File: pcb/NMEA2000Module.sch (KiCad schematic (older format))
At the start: 45 parts, among them IC1 MCP2562FD, K1 1W1, P1 PULSE_IN, P3 TERM_R, P4 CAN, P7 I2C1, P9 ANALOG IN, SW1 BT Enable, U1 74HC14, U2 ESP32Dev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

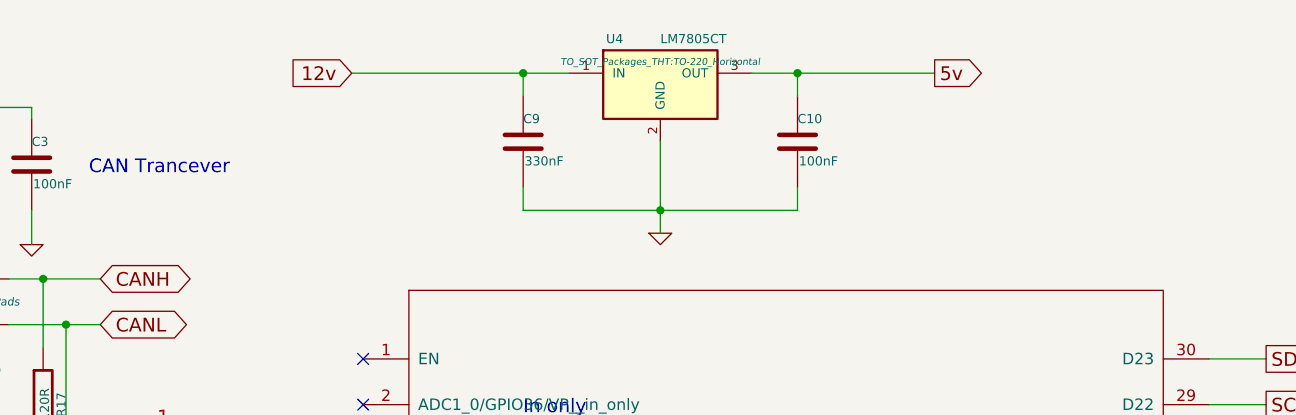
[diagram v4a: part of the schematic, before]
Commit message: Dropped oil pressure, teste fuel level
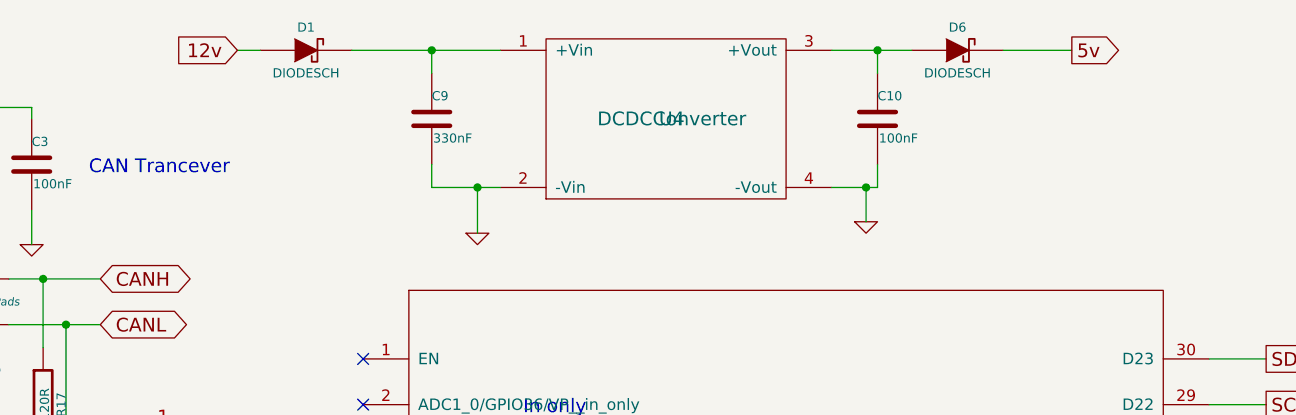
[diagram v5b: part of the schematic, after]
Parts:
- removed U4: LM7805CT, TO_SOT_Packages_THT:TO-220_Horizontal, symbol LM7805CT
- added D1, D6: DIODESCH, Resistors_ThroughHole:Resistor_Horizontal_RM7mm, symbol DIODESCH
- added U4: DCDCConverter, Divers:DC-DC-Converter, symbol DCDCConverter
- D2, D3, D4, D5: footprint Resistors_ThroughHole:Resistor_Horizontal_RM7mm -> TO_SOT_Packages_SMD:SOT-23
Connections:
- net 12v: now also D1.1 (A); no longer C9.1
- net 5v: now also D6.2 (K); no longer C10.1
- net GND: now also U4.2 (-Vin), U4.4 (-Vout)
- new net: C9.1, D1.2 (K), U4.1 (+Vin)
- new net: C10.1, D6.1 (A), U4.3 (+Vout)
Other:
- moved on the sheet: C10, C9
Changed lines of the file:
@@
 Text GLabel 3450 5050 0    60   Input ~ 0
 5v
-Text GLabel 6200 900  2    60   Output ~ 0
+Text GLabel 6800 800  2    60   Output ~ 0
 5v
 $Comp
@@
 Text GLabel 10500 4100 2    60   BiDi ~ 0
 CANL
-Text GLabel 3650 900  0    60   Input ~ 0
+Text GLabel 3150 800  0    60   Input ~ 0
 12v
 $Comp
 L GND #PWR014
 U 1 1 6019290E
-P 5000 1600
-F 0 "#PWR014" H 5000 1600 30  0001 C CNN
-F 1 "GND" H 5000 1530 30  0001 C CNN
-F 2 "" H 5000 1600 60  0001 C CNN
-F 3 "" H 5000 1600 60  0001 C CNN
-	1    5000 1600
+P 4200 1600
+F 0 "#PWR014" H 4200 1600 30  0001 C CNN
+F 1 "GND" H 4200 1530 30  0001 C CNN
+F 2 "" H 4200 1600 60  0001 C CNN
+F 3 "" H 4200 1600 60  0001 C CNN
+	1    4200 1600
 	1    0    0    -1
 $EndComp
@@
 F 0 "D3" H 1000 7500 40  0000 C CNN
 F 1 "DIODE" H 1000 7300 40  0000 C CNN
-F 2 "Resistors_ThroughHole:Resistor_Horizontal_RM7mm" H 1000 7400 60  0001 C CNN
+F 2 "TO_SOT_Packages_SMD:SOT-23" H 1000 7400 60  0001 C CNN
 F 3 "" H 1000 7400 60  0000 C CNN
 	1    1000 7400
@@
 F 0 "D2" H 1000 6850 40  0000 C CNN
 F 1 "DIODE" H 1000 6650 40  0000 C CNN
-F 2 "Resistors_ThroughHole:Resistor_Horizontal_RM7mm" H 1000 6750 60  0001 C CNN
+F 2 "TO_SOT_Packages_SMD:SOT-23" H 1000 6750 60  0001 C CNN
 F 3 "" H 1000 6750 60  0000 C CNN
 	1    1000 6750
@@
 F 0 "D5" H 3450 7500 40  0000 C CNN
 F 1 "DIODE" H 3450 7300 40  0000 C CNN
-F 2 "Resistors_ThroughHole:Resistor_Horizontal_RM7mm" H 3450 7400 60  0001 C CNN
+F 2 "TO_SOT_Packages_SMD:SOT-23" H 3450 7400 60  0001 C CNN
 F 3 "" H 3450 7400 60  0000 C CNN
 	1    3450 7400
@@
 F 0 "D4" H 3450 6900 40  0000 C CNN
 F 1 "DIODE" H 3450 6700 40  0000 C CNN
-F 2 "Resistors_ThroughHole:Resistor_Horizontal_RM7mm" H 3450 6800 60  0001 C CNN
+F 2 "TO_SOT_Packages_SMD:SOT-23" H 3450 6800 60  0001 C CNN
 F 3 "" H 3450 6800 60  0000 C CNN
 	1    3450 6800
@@
 	2650 3600 2500 3600
 Wire Wire Line
-	3650 900  4600 900
-Wire Wire Line
-	5400 900  6200 900
-Wire Wire Line
 	9950 4750 9950 4800
 Wire Wire Line
@@
 L C C9
 U 1 1 603DE009
-P 4400 1200
-F 0 "C9" H 4400 1300 40  0000 L CNN
-F 1 "330nF" H 4406 1115 40  0000 L CNN
-F 2 "Capacitors_SMD:C_0805_HandSoldering" H 4438 1050 30  0001 C CNN
-F 3 "" H 4400 1200 60  0000 C CNN
-	1    4400 1200
+P 4000 1100
+F 0 "C9" H 4000 1200 40  0000 L CNN
+F 1 "330nF" H 4006 1015 40  0000 L CNN
+F 2 "Capacitors_SMD:C_0805_HandSoldering" H 4038 950 30  0001 C CNN
+F 3 "" H 4000 1100 60  0000 C CNN
+	1    4000 1100
 	1    0    0    -1
 $EndComp
@@
 L C C10
 U 1 1 603DE0BF
-P 5600 1200
-F 0 "C10" H 5600 1300 40  0000 L CNN
-F 1 "100nF" H 5606 1115 40  0000 L CNN
-F 2 "Capacitors_SMD:C_0805_HandSoldering" H 5638 1050 30  0001 C CNN
-F 3 "" H 5600 1200 60  0000 C CNN
-	1    5600 1200
-	1    0    0    -1
-$EndComp
-Wire Wire Line
-	4400 1400 4400 1500
-Wire Wire Line
-	4400 1500 5600 1500
-Wire Wire Line
-	5600 1500 5600 1400
-Wire Wire Line
-	5000 1200 5000 1600
-Connection ~ 5000 1500
-Wire Wire Line
-	4400 1000 4400 900
-Connection ~ 4400 900
-Wire Wire Line
-	5600 1000 5600 900
-Connection ~ 5600 900
-$Comp
-L LM7805CT U4
-U 1 1 603DFA56
-P 5000 950
-F 0 "U4" H 4800 1150 40  0000 C CNN
-F 1 "LM7805CT" H 5000 1150 40  0000 L CNN
-F 2 "TO_SOT_Packages_THT:TO-220_Horizontal" H 5000 1050 30  0000 C CIN
-F 3 "" H 5000 950 60  0000 C CNN
-	1    5000 950
+P 5950 1100
+F 0 "C10" H 5950 1200 40  0000 L CNN
+F 1 "100nF" H 5956 1015 40  0000 L CNN
+F 2 "Capacitors_SMD:C_0805_HandSoldering" H 5988 950 30  0001 C CNN
+F 3 "" H 5950 1100 60  0000 C CNN
+	1    5950 1100
 	1    0    0    -1
 $EndComp
@@
 Wire Wire Line
 	3550 3550 3700 3550
+$Comp
+L DCDCConverter U4
+U 1 1 6049D818
+P 5050 1100
+F 0 "U4" H 5050 1100 60  0000 C CNN
+F 1 "DCDCConverter" H 5050 1100 60  0000 C CNN
+F 2 "Divers:DC-DC-Converter" H 5050 1100 60  0001 C CNN
+F 3 "" H 5050 1100 60  0001 C CNN
+	1    5050 1100
+	1    0    0    -1
+$EndComp
+Wire Wire Line
+	4300 800  3650 800
+Wire Wire Line
+	4000 900  4000 800
+Connection ~ 4000 800
+Wire Wire Line
+	5950 900  5950 800
+Wire Wire Line
+	5750 800  6100 800
+Wire Wire Line
+	5950 1300 5950 1400
+Wire Wire Line
+	5950 1400 5750 1400
+Wire Wire Line
+	4300 1400 4000 1400
+Wire Wire Line
+	4000 1400 4000 1300
+Wire Wire Line
+	4200 1600 4200 1400
+Connection ~ 4200 1400
+$Comp
+L DIODESCH D1
+U 1 1 6049E8CA
+P 3450 800
+F 0 "D1" H 3450 900 40  0000 C CNN
+F 1 "DIODESCH" H 3450 700 40  0000 C CNN
+F 2 "Resistors_ThroughHole:Resistor_Horizontal_RM7mm" H 3450 800 60  0001 C CNN
+F 3 "" H 3450 800 60  0000 C CNN
+	1    3450 800
+	1    0    0    -1
+$EndComp
+$Comp
+L DIODESCH D6
+U 1 1 6049E984
+P 6300 800
+F 0 "D6" H 6300 900 40  0000 C CNN
+F 1 "DIODESCH" H 6300 700 40  0000 C CNN
+F 2 "Resistors_ThroughHole:Resistor_Horizontal_RM7mm" H 6300 800 60  0001 C CNN
+F 3 "" H 6300 800 60  0000 C CNN
+	1    6300 800
+	1    0    0    -1
+$EndComp
+Connection ~ 5950 800
+Wire Wire Line
+	6500 800  6800 800
+Wire Wire Line
+	3250 800  3150 800
+$Comp
+L GND #PWR018
+U 1 1 6049ED9D
+P 5900 1550
+F 0 "#PWR018" H 5900 1550 30  0001 C CNN
+F 1 "GND" H 5900 1480 30  0001 C CNN
+F 2 "" H 5900 1550 60  0001 C CNN
+F 3 "" H 5900 1550 60  0001 C CNN
+	1    5900 1550
+	1    0    0    -1
+$EndComp
+Wire Wire Line
+	5900 1550 5900 1400
+Connection ~ 5900 1400
 $EndSCHEMATC

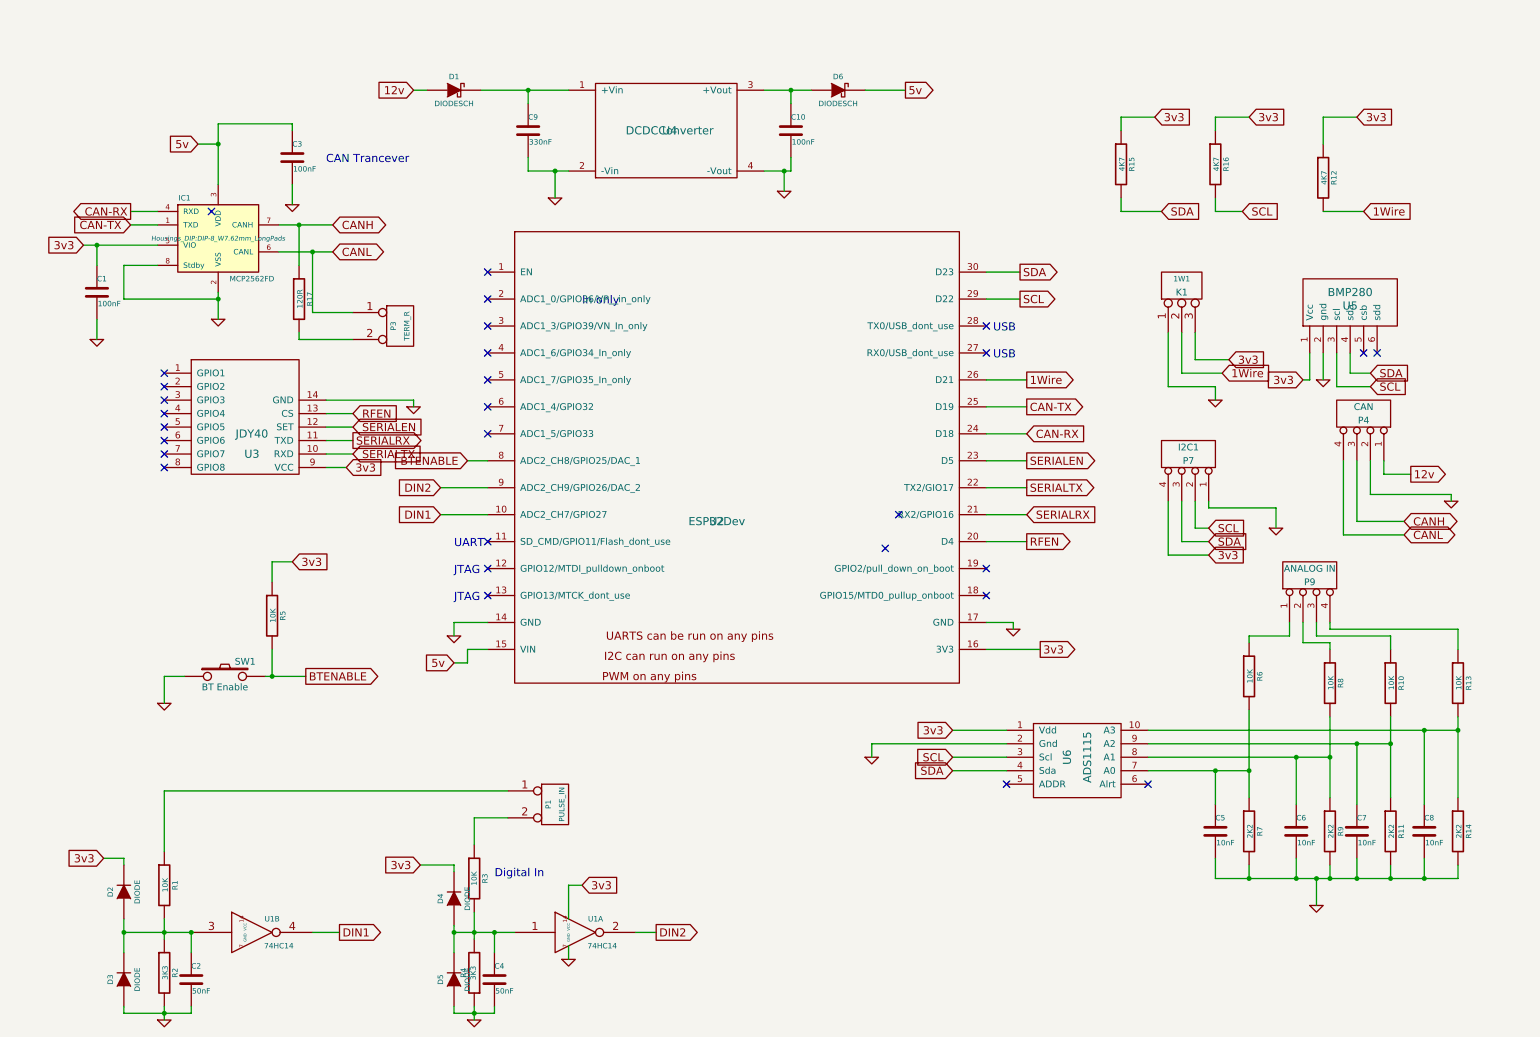
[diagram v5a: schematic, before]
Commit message: Added better support for simulation and alarms
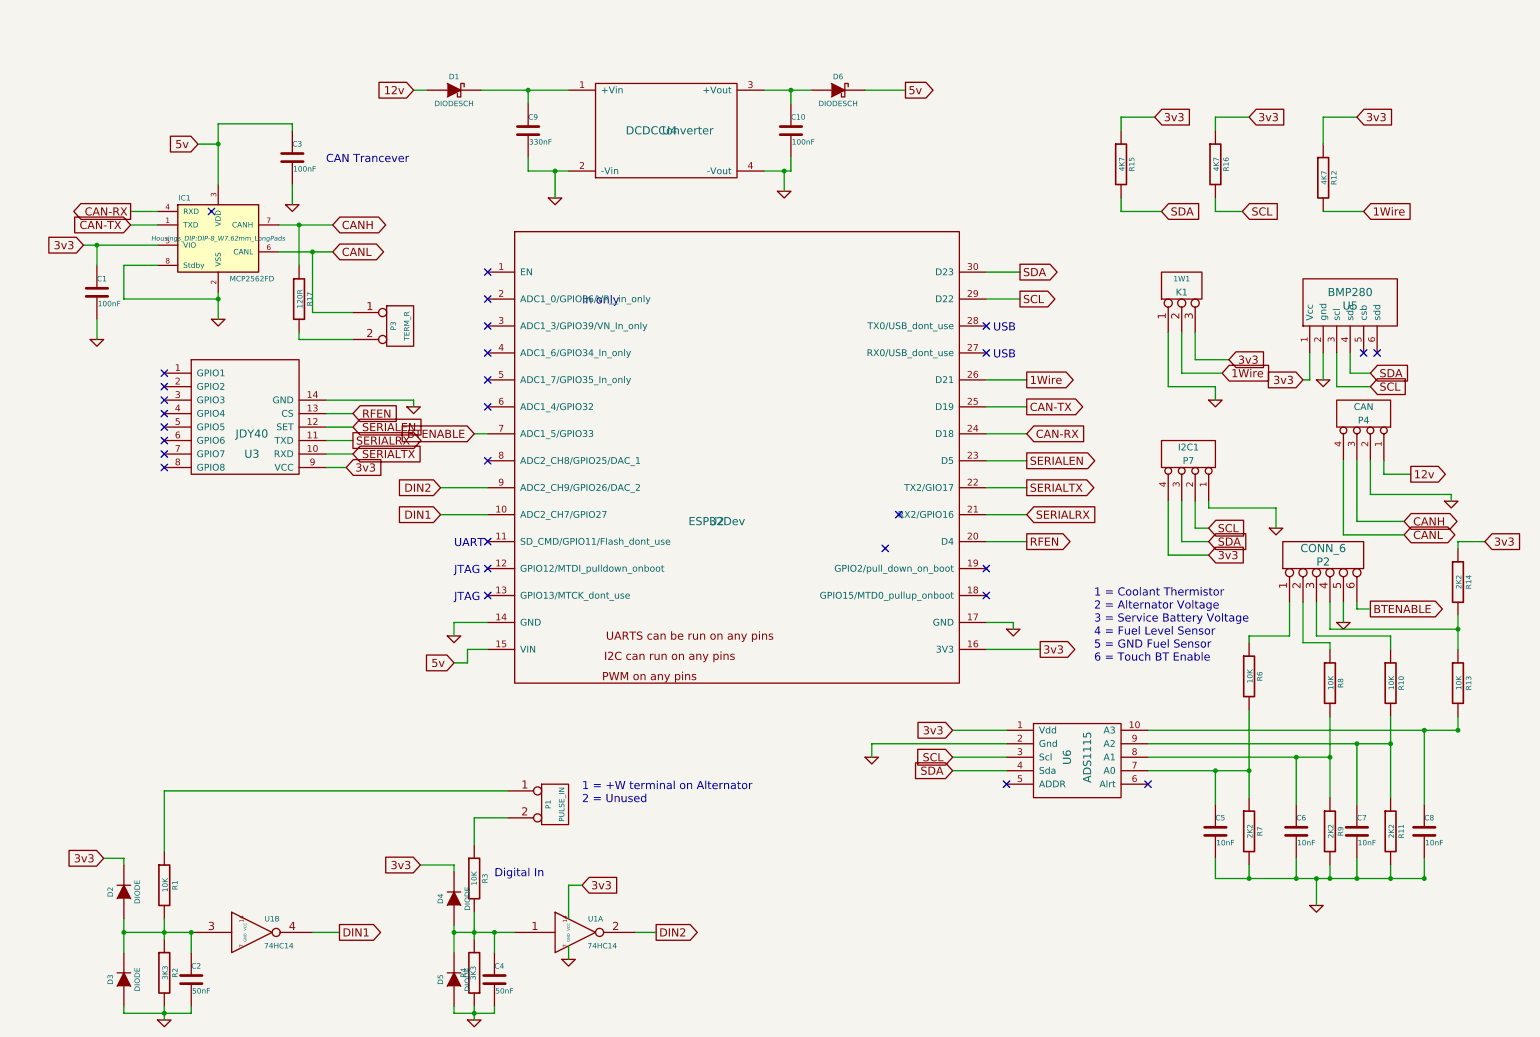
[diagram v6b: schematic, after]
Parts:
- removed P9: ANALOG IN, Pin_Headers:Pin_Header_Straight_1x04_Pitch2.54mm, symbol CONN_4
- removed R5: 10K, Resistors_SMD:R_0805_HandSoldering, symbol R
- removed SW1: BT Enable, Buttons_Switches_ThroughHole:SW_PUSH_6mm, symbol SW_PUSH
- added P2: CONN_6, Pin_Headers:Pin_Header_Straight_1x06_Pitch2.54mm, symbol CONN_6
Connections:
- net 3v3: now also R14.1
- net BTENABLE: now also U2.7 (ADC1_5/GPIO33), P2.6; no longer U2.8 (ADC2_CH8/GPIO25/DAC_1)
- net GND: now also P2.5; no longer R14.2
- net at R8.1: now also P2.2
- net at R10.1: now also P2.3
- net at R13.1: now also R14.2, P2.4
- net at C8.1, R13.2, U6.10 (A3): no longer R14.1
- net at R6.1: now also P2.1
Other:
- note added: "1 = +W terminal on Alternator\n2 = Unused"
- note added: "1 = Coolant Thermistor\n2 = Alternator Voltage\n3 = Service Battery Voltage\n4 = Fuel Level Sensor\n5 = GND Fuel Sensor\n6 = Touch BT Enable\n"
- moved on the sheet: R14
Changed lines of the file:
@@
-$EndComp
-$Comp
-L CONN_4 P9
-U 1 1 5F40035E
-P 9800 4400
-F 0 "P9" V 9750 4400 50  0000 C CNN
-F 1 "ANALOG IN" V 9850 4400 50  0000 C CNN
-F 2 "Pin_Headers:Pin_Header_Straight_1x04_Pitch2.54mm" H 9800 4400 60  0001 C CNN
-F 3 "" H 9800 4400 60  0001 C CNN
-	1    9800 4400
-	0    -1   -1   0
 $EndComp
 $Comp
@@
 NoConn ~ 7400 4550
 NoConn ~ 7400 4350
-NoConn ~ 3700 3350
 NoConn ~ 3700 3150
 NoConn ~ 3700 2950
@@
 L R R14
 U 1 1 60181295
-P 10900 6300
-F 0 "R14" V 10980 6300 40  0000 C CNN
-F 1 "2K2" V 10907 6301 40  0000 C CNN
-F 2 "Resistors_SMD:R_0805_HandSoldering" V 10830 6300 30  0001 C CNN
-F 3 "" H 10900 6300 30  0000 C CNN
-	1    10900 6300
+P 10900 4450
+F 0 "R14" V 10980 4450 40  0000 C CNN
+F 1 "2K2" V 10907 4451 40  0000 C CNN
+F 2 "Resistors_SMD:R_0805_HandSoldering" V 10830 4450 30  0001 C CNN
+F 3 "" H 10900 4450 30  0000 C CNN
+	1    10900 4450
 	1    0    0    -1
 $EndComp
@@
 	2650 3600 2500 3600
 Wire Wire Line
-	9950 4750 9950 4800
+	9950 4600 9950 4800
 Wire Wire Line
 	9950 4800 10900 4800
 Wire Wire Line
-	10900 4800 10900 4950
-Wire Wire Line
-	10400 4950 10400 4850
-Wire Wire Line
-	10400 4850 9850 4850
-Wire Wire Line
-	9850 4850 9850 4750
+	10900 4700 10900 4950
+Wire Wire Line
+	10400 4850 10400 4950
+Wire Wire Line
+	9850 4600 9850 4850
 Wire Wire Line
 	9950 4950 9950 4900
@@
 	9950 4900 9750 4900
 Wire Wire Line
-	9750 4900 9750 4750
+	9750 4900 9750 4600
 Wire Wire Line
 	9350 4900 9350 4850
@@
 	9350 4850 9650 4850
 Wire Wire Line
-	9650 4850 9650 4750
+	9650 4850 9650 4600
 Wire Wire Line
 	9100 6500 9100 6650
 Wire Wire Line
-	9100 6650 10900 6650
-Wire Wire Line
-	10900 6650 10900 6550
+	9100 6650 10650 6650
 Wire Wire Line
 	10650 6650 10650 6500
@@
 	8600 5550 10900 5550
 Wire Wire Line
-	10900 5450 10900 6050
+	10900 5550 10900 5450
 Wire Wire Line
 	8600 5650 10400 5650
@@
 	1    0    0    -1
 $EndComp
-$Comp
-L SW_PUSH SW1
-U 1 1 6049C3C9
-P 1750 5150
-F 0 "SW1" H 1900 5260 50  0000 C CNN
-F 1 "BT Enable" H 1750 5070 50  0000 C CNN
-F 2 "Buttons_Switches_ThroughHole:SW_PUSH_6mm" H 1750 5150 60  0001 C CNN
-F 3 "" H 1750 5150 60  0000 C CNN
-	1    1750 5150
-	1    0    0    -1
-$EndComp
-$Comp
-L R R5
-U 1 1 6049C957
-P 2100 4700
-F 0 "R5" V 2180 4700 40  0000 C CNN
-F 1 "10K" V 2107 4701 40  0000 C CNN
-F 2 "Resistors_SMD:R_0805_HandSoldering" V 2030 4700 30  0001 C CNN
-F 3 "" H 2100 4700 30  0000 C CNN
-	1    2100 4700
-	1    0    0    -1
-$EndComp
-$Comp
-L GND #PWR017
-U 1 1 6049C9FC
-P 1300 5350
-F 0 "#PWR017" H 1300 5350 30  0001 C CNN
-F 1 "GND" H 1300 5280 30  0001 C CNN
-F 2 "" H 1300 5350 60  0001 C CNN
-F 3 "" H 1300 5350 60  0001 C CNN
-	1    1300 5350
-	1    0    0    -1
-$EndComp
-Wire Wire Line
-	1450 5150 1300 5150
-Wire Wire Line
-	1300 5150 1300 5350
-Wire Wire Line
-	2050 5150 2350 5150
-Wire Wire Line
-	2100 5150 2100 4950
-Text GLabel 2250 4300 2    60   Input ~ 0
-3v3
-Wire Wire Line
-	2100 4450 2100 4300
-Wire Wire Line
-	2100 4300 2250 4300
-Text GLabel 3550 3550 0    60   Input ~ 0
+Text GLabel 3600 3350 0    60   Input ~ 0
 BTENABLE
-Text GLabel 2350 5150 2    60   Output ~ 0
+Text GLabel 10250 4650 2    60   Output ~ 0
 BTENABLE
-Connection ~ 2100 5150
-Wire Wire Line
-	3550 3550 3700 3550
 $Comp
 L DCDCConverter U4
@@
 $EndComp
 Wire Wire Line
-	4300 800  3650 800
+	3650 800  4300 800
 Wire Wire Line
 	4000 900  4000 800
@@
 	5750 800  6100 800
 Wire Wire Line
-	5950 1300 5950 1400
-Wire Wire Line
-	5950 1400 5750 1400
-Wire Wire Line
-	4300 1400 4000 1400
+	5950 1400 5950 1300
+Wire Wire Line
+	5750 1400 5950 1400
+Wire Wire Line
+	4000 1400 4300 1400
 Wire Wire Line
 	4000 1400 4000 1300
@@
 	3250 800  3150 800
 $Comp
-L GND #PWR018
+L GND #PWR017
 U 1 1 6049ED9D
 P 5900 1550
-F 0 "#PWR018" H 5900 1550 30  0001 C CNN
+F 0 "#PWR017" H 5900 1550 30  0001 C CNN
 F 1 "GND" H 5900 1480 30  0001 C CNN
 F 2 "" H 5900 1550 60  0001 C CNN
@@
 	5900 1550 5900 1400
 Connection ~ 5900 1400
+Wire Wire Line
+	3600 3350 3700 3350
+NoConn ~ 3700 3550
+Text GLabel 11100 4150 2    60   Input ~ 0
+3v3
+Text Notes 8200 5050 0    60   ~ 0
+1 = Coolant Thermistor\n2 = Alternator Voltage\n3 = Service Battery Voltage\n4 = Fuel Level Sensor\n5 = GND Fuel Sensor\n6 = Touch BT Enable\n
+Wire Wire Line
+	11100 4150 10900 4150
+Wire Wire Line
+	10900 4150 10900 4200
+Connection ~ 10900 4800
+Wire Wire Line
+	9850 4850 10400 4850
+Text Notes 4400 6100 0    60   ~ 0
+1 = +W terminal on Alternator\n2 = Unused
+$Comp
+L CONN_6 P2
+U 1 1 605B485A
+P 9900 4250
+F 0 "P2" V 9850 4250 60  0000 C CNN
+F 1 "CONN_6" V 9950 4250 60  0000 C CNN
+F 2 "Pin_Headers:Pin_Header_Straight_1x06_Pitch2.54mm" H 9900 4250 60  0001 C CNN
+F 3 "" H 9900 4250 60  0001 C CNN
+	1    9900 4250
+	0    -1   -1   0
+$EndComp
+$Comp
+L GND #PWR018
+U 1 1 605B4A3A
+P 10050 4750
+F 0 "#PWR018" H 10050 4750 30  0001 C CNN
+F 1 "GND" H 10050 4680 30  0001 C CNN
+F 2 "" H 10050 4750 60  0001 C CNN
+F 3 "" H 10050 4750 60  0001 C CNN
+	1    10050 4750
+	1    0    0    -1
+$EndComp
+Wire Wire Line
+	10050 4600 10050 4750
+Wire Wire Line
+	10150 4600 10150 4650
+Wire Wire Line
+	10150 4650 10250 4650
 $EndSCHEMATC

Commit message: Update to pcb to reflect prototype
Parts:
- added R5: 10K, Resistors_SMD:R_0805_HandSoldering, symbol R
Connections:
- net 3v3: now also R5.1
- net BTENABLE: now also U2.8 (ADC2_CH8/GPIO25/DAC_1), R5.2; no longer U2.7 (ADC1_5/GPIO33)
